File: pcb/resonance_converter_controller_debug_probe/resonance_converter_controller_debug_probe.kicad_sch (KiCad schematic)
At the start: 0 parts

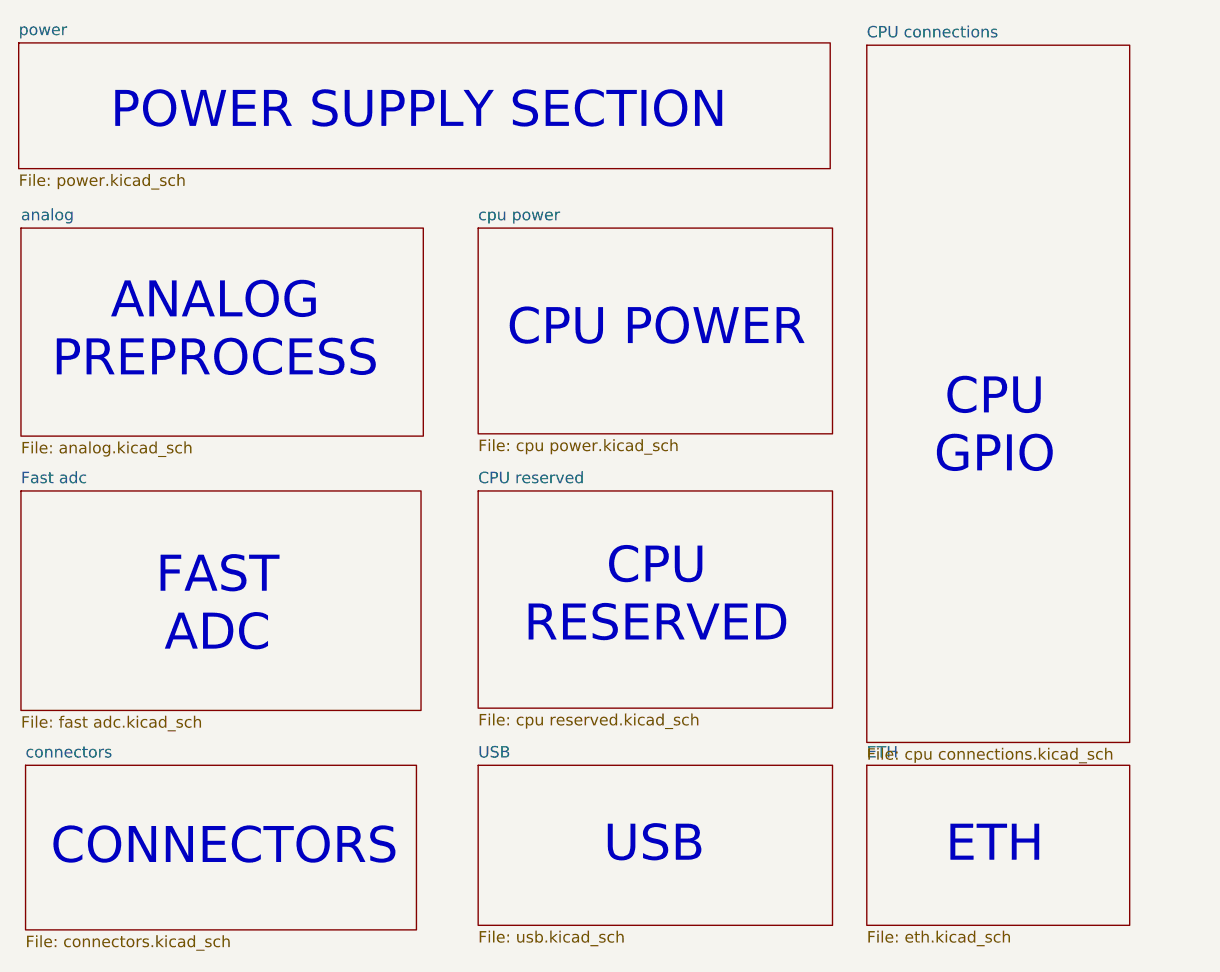
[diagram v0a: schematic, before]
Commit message: Add schematic for debug probe
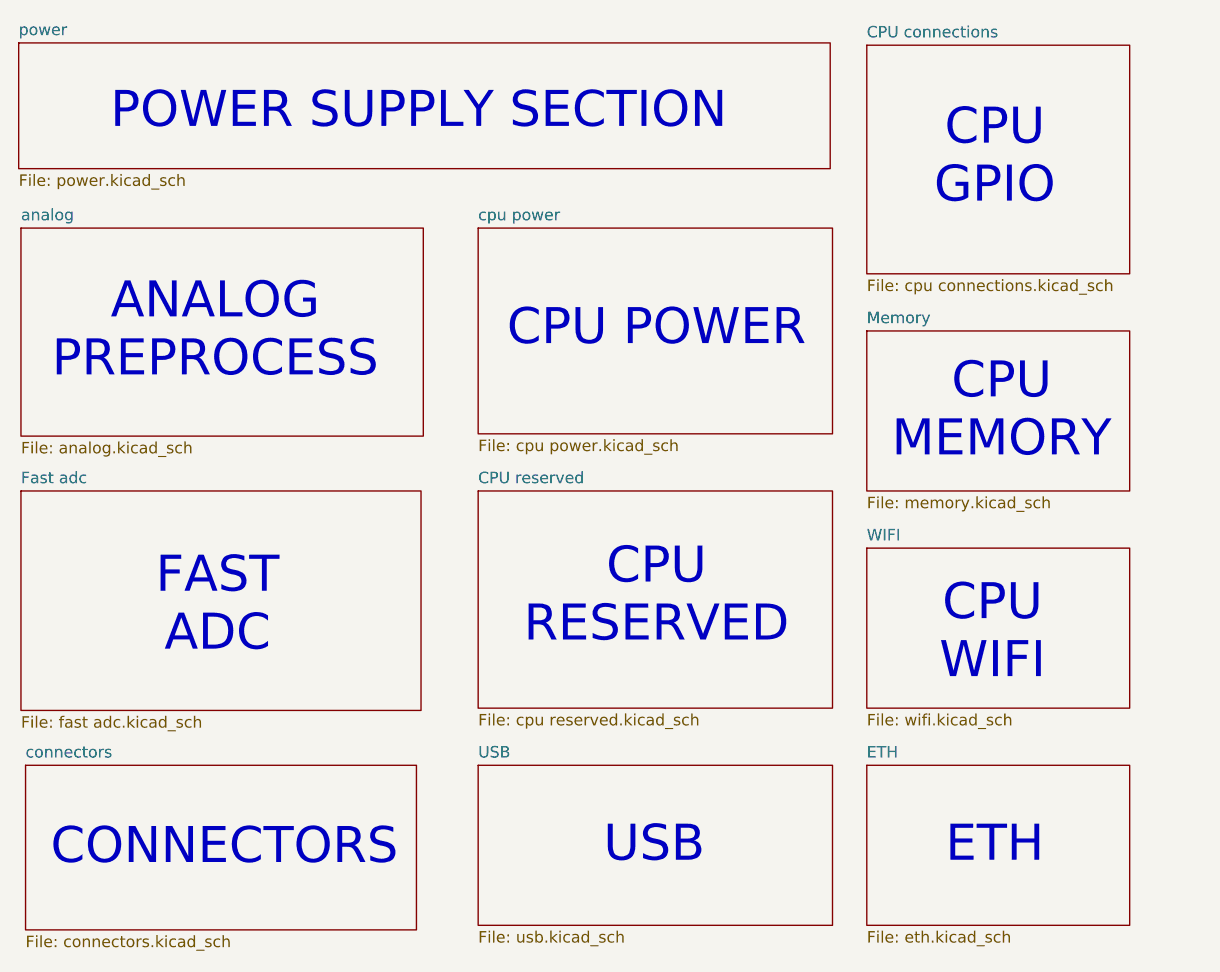
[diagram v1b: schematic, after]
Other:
- added sheet Memory (memory.kicad_sch)
- added sheet WIFI (wifi.kicad_sch)
- note added: "CPU MEMORY"
- note added: "CPU WIFI"
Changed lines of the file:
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@@
 	(text "CPU\nGPIO"
 		(exclude_from_sim no)
-		(at 194.564 91.948 0)
+		(at 194.564 61.976 0)
 		(effects
 			(font
@@
 		)
 	)
+	(text "CPU\nMEMORY"
+		(exclude_from_sim no)
+		(at 195.326 90.17 0)
+		(effects
+			(font
+				(size 4 4)
+			)
+		)
+	)
 	(text "USB"
 		(exclude_from_sim no)
@@
 		(exclude_from_sim no)
 		(at 156.972 81.026 0)
+		(effects
+			(font
+				(size 4 4)
+			)
+		)
+	)
+	(text "CPU\nWIFI"
+		(exclude_from_sim no)
+		(at 194.31 114.808 0)
 		(effects
 			(font
@@
 	(sheet
 		(at 180.34 49.53)
-		(size 29.21 77.47)
+		(size 29.21 25.4)
 		(exclude_from_sim no)
 		(in_bom yes)
@@
 		)
 		(property "Sheetfile" "cpu connections.kicad_sch"
-			(at 180.34 127.5846 0)
+			(at 180.34 75.5146 0)
 			(effects
 				(font
@@
 				)
 			)
+		)
+	)
+	(sheet
+		(at 180.34 81.28)
+		(size 29.21 17.78)
+		(exclude_from_sim no)
+		(in_bom yes)
+		(on_board yes)
+		(dnp no)
+		(fields_autoplaced yes)
+		(stroke
+			(width 0.1524)
+			(type solid)
+		)
+		(fill
+			(color 0 0 0 0.0000)
+		)
+		(property "Sheetname" "Memory"
+			(at 180.34 80.5684 0)
+			(effects
+				(font
+					(size 1.27 1.27)
+				)
+				(justify left bottom)
+			)
+		)
+		(property "Sheetfile" "memory.kicad_sch"
+			(at 180.34 99.6446 0)
+			(effects
+				(font
+					(size 1.27 1.27)
+				)
+				(justify left top)
+			)
+		)
+		(instances
+			(project "resonance_converter_controller_debug_probe"
+				(path "/09cfad33-2fee-4b03-99a1-883b8ac2919b"
+					(page "11")
+				)
+			)
+		)
+	)
+	(sheet
+		(at 180.34 105.41)
+		(size 29.21 17.78)
+		(exclude_from_sim no)
+		(in_bom yes)
+		(on_board yes)
+		(dnp no)
+		(fields_autoplaced yes)
+		(stroke
+			(width 0.1524)
+			(type solid)
+		)
+		(fill
+			(color 0 0 0 0.0000)
+		)
+		(property "Sheetname" "WIFI"
+			(at 180.34 104.6984 0)
+			(effects
+				(font
+					(size 1.27 1.27)
+				)
+				(justify left bottom)
+			)
+		)
+		(property "Sheetfile" "wifi.kicad_sch"
+			(at 180.34 123.7746 0)
+			(effects
+				(font
+					(size 1.27 1.27)
+				)
+				(justify left top)
+			)
+		)
+		(instances
+			(project "resonance_converter_controller_debug_probe"
+				(path "/09cfad33-2fee-4b03-99a1-883b8ac2919b"
+					(page "12")
+				)
+			)
